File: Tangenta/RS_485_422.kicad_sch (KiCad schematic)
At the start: 37 parts, among them Q3 BSS138, U21 TPCDSOT23-SM712, U22 TPCDSOT23-SM712

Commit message: ...
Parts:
- added C1 (x2): 10nF, Capacitor_SMD:C_0402_1005Metric, symbol Device:C_Small
- added J15: Conn_01x06_Pin, Connector_PinHeader_2.54mm:PinHeader_1x06_P2.54mm_Vertical, symbol Connector:Conn_01x06_Pin
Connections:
- net 5V: now also C1.2, C1.2
- net CTS_2_H: now also J15.3 (Pin_3)
- net GNDREF: now also C1.1, C1.1, J15.5 (Pin_5), J15.6 (Pin_6)
- net RTS_2_H: now also J15.2 (Pin_2)
- net RXD_2_H: now also J15.1 (Pin_1)
- net TXD_2_H: now also J15.4 (Pin_4)
- net RS485_CH_1.N: no longer names the net of R2.1, R2.1
- net RS485_CH_1.N: no longer U21.1
- net RS485_CH_1.P: no longer names the net of R2.1, R2.2
- net RS485_CH_1.P: no longer U21.2
- net RS485_CH_2.N: no longer names the net of R2.1, R2.1
- net RS485_CH_2.N: no longer U22.1
- net RS485_CH_2.P: no longer names the net of R2.1, R2.2
- net RS485_CH_2.P: no longer U22.2
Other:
- note added: "For future use"
- moved on the sheet: C1, R2, U21, U22

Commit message: ...
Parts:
- added U19: ADM2582E, Package_SO:SOIC-20W_7.5x12.8mm_P1.27mm, symbol Interface_UART:ADM2582E
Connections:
- net 5V: now also U19.2 (VCC), U19.8 (VCC); no longer C1.2, C1.2, C1.2
- net A: now also R2.2, U19.18 (A); no longer R2.2, R2.2
- net B: now also R2.2, U19.17 (B); no longer R2.2, R2.2
- net CTS_1_H: now also U19.6 (DE)
- net GNDREF: now also U19.1 (GND1), U19.10 (GND1), U19.3 (GND1), U19.9 (GND1); no longer C1.1, C1.1, C1.1, U21.3, U22.3
- net RTS_1_H: now also U19.5 (~{RE})
- net RXD_1_H: now also U19.4 (RxD)
- net TXD_1_H: now also U19.7 (TxD)
- net RS.R_P: now reaches R2.1, R2.1
- net RS.R_P: now also U22.1
- net RS.R_N: now reaches R2.1, R2.2
- net RS.R_N: now also U22.2
- net RS.D_P: now reaches R2.1, R2.2
- net RS.D_P: now also U21.2
- net RS.D_N: now reaches R2.1, R2.1
- net RS.D_N: now also U21.1
- new net RS_ISO_5V: C1.2, C1.2, C1.2, U19.12 (Visoout), U19.19 (Visoin)
- new net RS_ISO_GND: C1.1, C1.1, C1.1, U19.11 (GND2), U19.14 (GND2), U19.16 (GND2), U19.20 (GND2), U21.3, U22.3
- new net Y: R2.2, U19.13 (Y)
- new net Z: R2.2, U19.15 (Z)
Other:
- moved on the sheet: C1, J15, R2, U21, U22

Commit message: RS-485/422 revisited.
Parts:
- added J22: Conn_01x02_Pin, Connector_PinHeader_2.54mm:PinHeader_1x02_P2.54mm_Vertical, symbol Connector:Conn_01x02_Pin
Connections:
- net RS_ISO_GND: now also J22.2 (Pin_2)
- new net RS_CONN_GND: J22.1 (Pin_1)
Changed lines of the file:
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@@
+    (stroke (width 0) (type default))
+  )
+  (wire (pts (xy 248.92 135.89) (xy 252.73 135.89))
     (stroke (width 0) (type default))
   )
@@
     (stroke (width 0) (type default))
   )
+  (wire (pts (xy 246.38 135.89) (xy 227.965 135.89))
+    (stroke (width 0) (type default))
+  )
   (wire (pts (xy 133.985 42.545) (xy 137.795 42.545))
     (stroke (width 0) (type default))
@@
     (effects (font (size 1.27 1.27)) (justify right bottom))
   )
+  (label "RS_ISO_GND" (at 227.965 135.89 0) (fields_autoplaced)
+    (effects (font (size 1.27 1.27)) (justify left bottom))
+  )
   (label "5V" (at 42.545 27.305 0) (fields_autoplaced)
     (effects (font (size 1.27 1.27)) (justify left bottom))
@@
   (label "RS_ISO_GND" (at 243.84 41.91 180) (fields_autoplaced)
     (effects (font (size 1.27 1.27)) (justify right bottom))
+  )
+  (hierarchical_label "RS_CONN_GND" (shape bidirectional) (at 252.73 135.89 0) (fields_autoplaced)
+    (effects (font (size 1.27 1.27)) (justify left))
   )
   (hierarchical_label "UART_1{RXD TXD RTS CTS}" (shape input) (at 43.18 60.325 180) (fields_autoplaced)
@@
         )
       )
+    )
+  )
+  (symbol (lib_id "Connector:Conn_01x02_Pin") (at 248.92 130.81 270) (unit 1)
+    (in_bom yes) (on_board yes) (dnp no)
+    (property "Reference" "J22" (at 245.745 129.54 90)
+      (effects (font (size 1.27 1.27)) (justify left))
+    )
+    (property "Value" "Conn_01x02_Pin" (at 250.19 132.715 90)
+      (effects (font (size 1.27 1.27)) (justify left) hide)
+    )
+    (property "Footprint" "Connector_PinHeader_2.54mm:PinHeader_1x02_P2.54mm_Vertical" (at 248.92 130.81 0)
+      (effects (font (size 1.27 1.27)) hide)
+    )
+    (property "Datasheet" "~" (at 248.92 130.81 0)
+      (effects (font (size 1.27 1.27)) hide)
+    )
+    (pin "1")
+    (pin "2")
+    (instances
+      (project "Tangenta"
+        (path "/358d1bcf-7599-4352-8c4d-baa18a5f09e6/98e3b24f-9927-4339-b8fd-9deea91a522a"
+          (reference "J22") (unit 1)
+        )
+      )

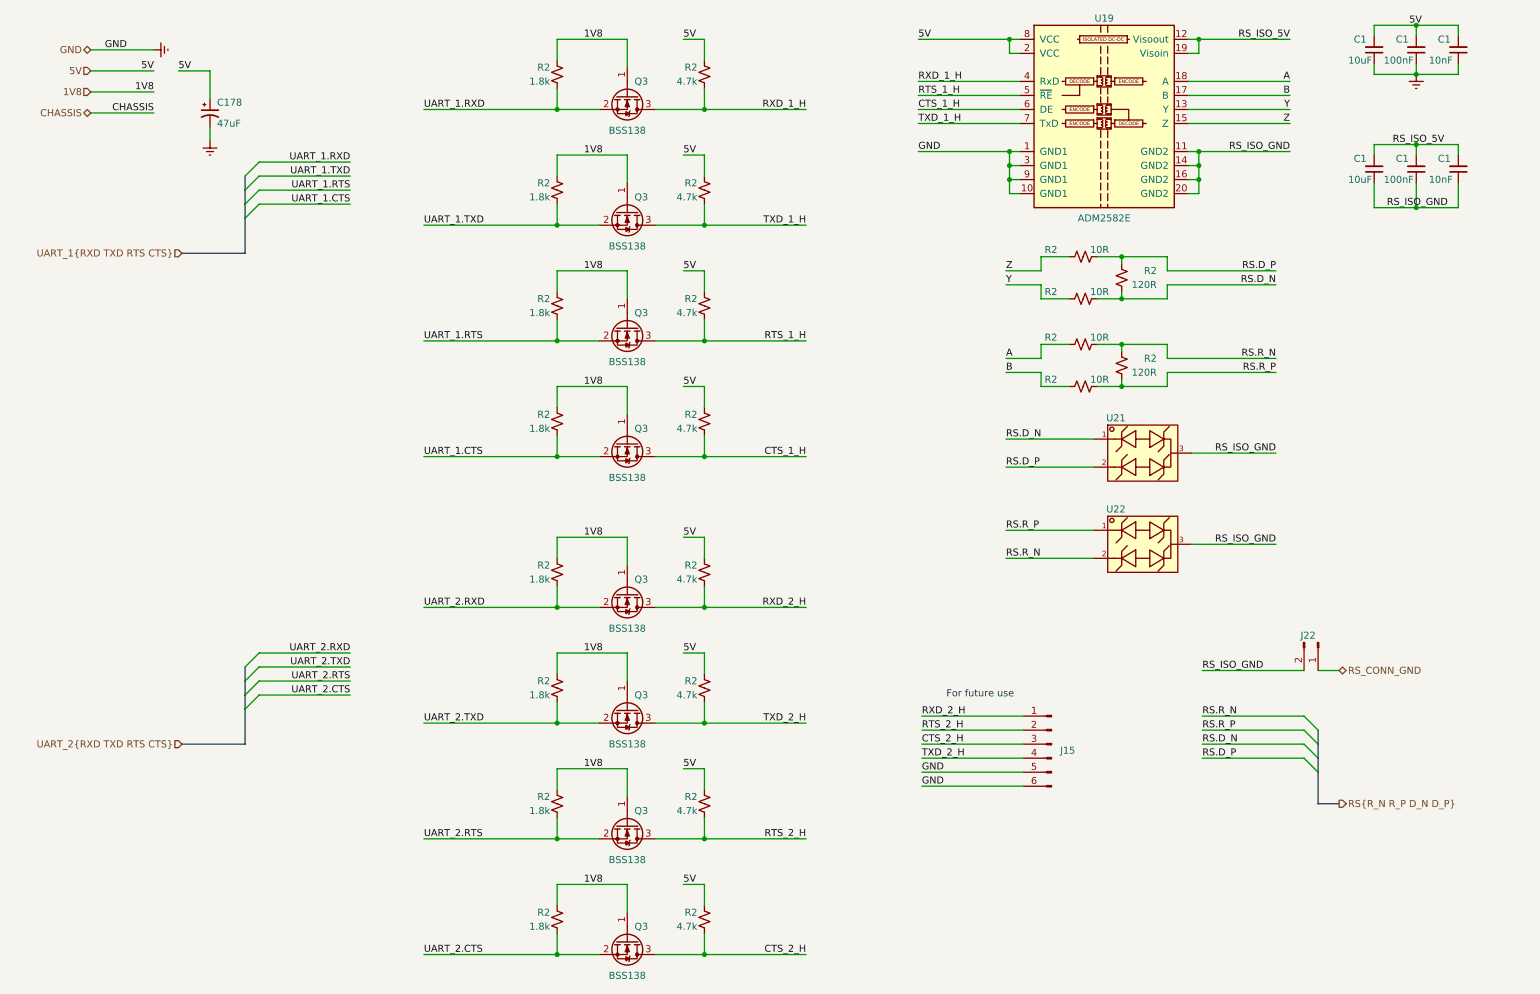
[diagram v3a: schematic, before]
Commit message: RS-485/422 schematics fine-tuned.
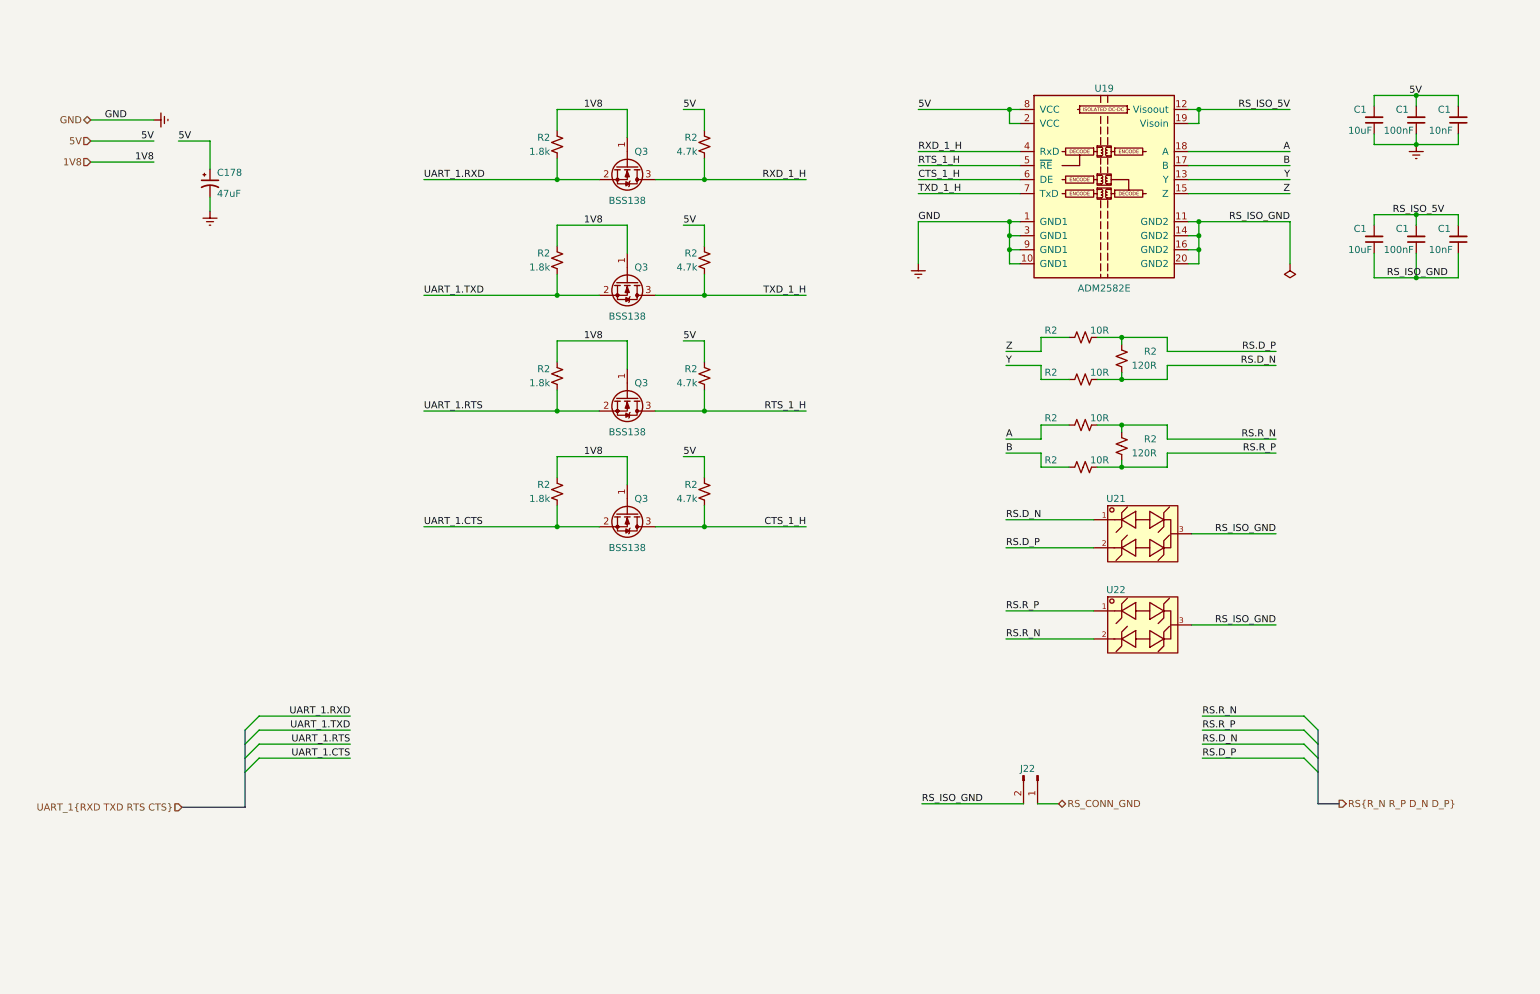
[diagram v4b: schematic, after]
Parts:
- removed J15: Conn_01x06_Pin, Connector_PinHeader_2.54mm:PinHeader_1x06_P2.54mm_Vertical, symbol Connector:Conn_01x06_Pin
- removed Q3 (x4): BSS138, Package_TO_SOT_SMD:SOT-23, symbol Transistor_FET:BSS138
- removed R2 (x4): 4.7k, Resistor_SMD:R_0402_1005Metric, symbol Device:R_Small_US
- removed R2 (x4): 1.8k, Resistor_SMD:R_0402_1005Metric, symbol Device:R_Small_US
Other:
- note removed: "For future use"
- moved on the sheet: C1, C178, J22, Q3, R2, U19, U21, U22

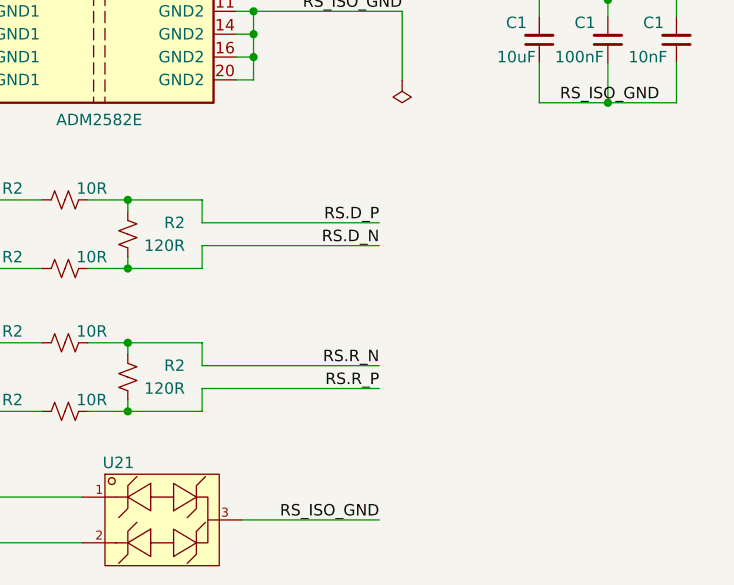
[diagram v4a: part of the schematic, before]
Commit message: Adding 0Rs for RS-485 configuration.
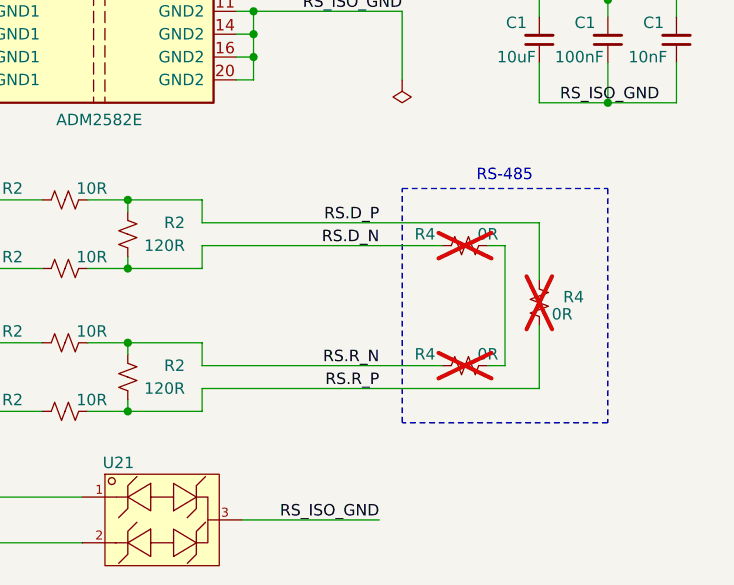
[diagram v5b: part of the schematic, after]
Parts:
- added R4 (x3): 0R, Resistor_SMD:R_0603_1608Metric, symbol Device:R_Small_US
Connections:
- net RS.D_N: now also R4.2
- net RS.D_P: now also R4.1
- net RS.R_N: now also R4.2
- net RS.R_P: now also R4.2
- new net: R4.1, R4.1
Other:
- note added: "RS-485"
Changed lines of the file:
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@@
     (stroke (width 0) (type default))
   )
-  (wire (pts (xy 221.615 93.98) (xy 241.3 93.98))
+  (wire (pts (xy 221.615 93.98) (xy 248.285 93.98))
     (stroke (width 0) (type default))
   )
@@
     (stroke (width 0) (type default))
   )
-  (wire (pts (xy 221.615 78.105) (xy 241.3 78.105))
+  (wire (pts (xy 221.615 78.105) (xy 259.08 78.105))
+    (stroke (width 0) (type default))
+  )
+  (wire (pts (xy 255.27 80.645) (xy 255.27 93.98))
     (stroke (width 0) (type default))
   )
@@
     (stroke (width 0) (type default))
   )
-  (wire (pts (xy 221.615 96.52) (xy 241.3 96.52))
+  (wire (pts (xy 221.615 96.52) (xy 259.08 96.52))
     (stroke (width 0) (type default))
   )
@@
     (stroke (width 0) (type default))
   )
-  (wire (pts (xy 221.615 80.645) (xy 241.3 80.645))
+  (wire (pts (xy 221.615 80.645) (xy 248.285 80.645))
     (stroke (width 0) (type default))
   )
@@
     (stroke (width 0) (type default))
   )
+  (wire (pts (xy 253.365 80.645) (xy 255.27 80.645))
+    (stroke (width 0) (type default))
+  )
   (bus (pts (xy 43.18 160.655) (xy 54.61 160.655))
     (stroke (width 0) (type default))
@@
     (stroke (width 0) (type default))
   )
+  (wire (pts (xy 259.08 89.535) (xy 259.08 96.52))
+    (stroke (width 0) (type default))
+  )
   (wire (pts (xy 221.615 75.565) (xy 221.615 78.105))
     (stroke (width 0) (type default))
@@
     (stroke (width 0) (type default))
   )
+  (wire (pts (xy 255.27 93.98) (xy 253.365 93.98))
+    (stroke (width 0) (type default))
+  )
   (wire (pts (xy 198.755 80.645) (xy 198.755 83.185))
     (stroke (width 0) (type default))
@@
   (wire (pts (xy 192.405 93.98) (xy 198.755 93.98))
     (stroke (width 0) (type default))
+  )
+  (wire (pts (xy 259.08 84.455) (xy 259.08 78.105))
+    (stroke (width 0) (type default))
+  )
+  (rectangle (start 243.84 74.295) (end 266.7 100.33)
+    (stroke (width 0) (type dash))
+    (fill (type none))
+  )
+  (text "RS-485" (at 252.095 73.66 0)
+    (effects (font (size 1.27 1.27)) (justify left bottom))
   )
   (label "GND" (at 176.53 54.61 0) (fields_autoplaced)
@@
     )
   )
+  (symbol (lib_id "Device:R_Small_US") (at 250.825 80.645 270) (unit 1)
+    (in_bom no) (on_board yes) (dnp yes)
+    (property "Reference" "R4" (at 246.38 79.375 90)
+      (effects (font (size 1.27 1.27)))
+    )
+    (property "Value" "0R" (at 253.365 79.375 90)
+      (effects (font (size 1.27 1.27)))
+    )
+    (property "Footprint" "Resistor_SMD:R_0603_1608Metric" (at 250.825 80.645 0)
+      (effects (font (size 1.27 1.27)) hide)
+    )
+    (property "Datasheet" "~" (at 250.825 80.645 0)
+      (effects (font (size 1.27 1.27)) hide)
+    )
+    (pin "1")
+    (pin "2")
+    (instances
+      (project "Tangenta"
+        (path "/358d1bcf-7599-4352-8c4d-baa18a5f09e6/8215796b-9611-4f43-bcc5-319f8414b8a6"
+          (reference "R4") (unit 1)
+        )
+        (path "/358d1bcf-7599-4352-8c4d-baa18a5f09e6/98e3b24f-9927-4339-b8fd-9deea91a522a"
+          (reference "R171") (unit 1)
+        )
+      )
+    )
+  )
   (symbol (lib_id "Device:R_Small_US") (at 137.795 82.55 180) (unit 1)
     (in_bom yes) (on_board yes) (dnp no)
@@
         (path "/358d1bcf-7599-4352-8c4d-baa18a5f09e6/98e3b24f-9927-4339-b8fd-9deea91a522a"
           (reference "R170") (unit 1)
+        )
+      )
+    )
+  )
+  (symbol (lib_id "Device:R_Small_US") (at 259.08 86.995 0) (unit 1)
+    (in_bom no) (on_board yes) (dnp yes)
+    (property "Reference" "R4" (at 262.89 86.36 0)
+      (effects (font (size 1.27 1.27)))
+    )
+    (property "Value" "0R" (at 261.62 88.265 0)
+      (effects (font (size 1.27 1.27)))
+    )
+    (property "Footprint" "Resistor_SMD:R_0603_1608Metric" (at 259.08 86.995 0)
+      (effects (font (size 1.27 1.27)) hide)
+    )
+    (property "Datasheet" "~" (at 259.08 86.995 0)
+      (effects (font (size 1.27 1.27)) hide)
+    )
+    (pin "1")
+    (pin "2")
+    (instances
+      (project "Tangenta"
+        (path "/358d1bcf-7599-4352-8c4d-baa18a5f09e6/8215796b-9611-4f43-bcc5-319f8414b8a6"
+          (reference "R4") (unit 1)
+        )
+        (path "/358d1bcf-7599-4352-8c4d-baa18a5f09e6/98e3b24f-9927-4339-b8fd-9deea91a522a"
+          (reference "R173") (unit 1)
         )
       )
@@
         )
       )
+    )
+  )
+  (symbol (lib_id "Device:R_Small_US") (at 250.825 93.98 270) (unit 1)
+    (in_bom no) (on_board yes) (dnp yes)
+    (property "Reference" "R4" (at 246.38 92.71 90)
+      (effects (font (size 1.27 1.27)))
+    )
+    (property "Value" "0R" (at 253.365 92.71 90)
+      (effects (font (size 1.27 1.27)))
+    )
+    (property "Footprint" "Resistor_SMD:R_0603_1608Metric" (at 250.825 93.98 0)
+      (effects (font (size 1.27 1.27)) hide)
+    )
+    (property "Datasheet" "~" (at 250.825 93.98 0)
+      (effects (font (size 1.27 1.27)) hide)
+    )
+    (pin "1")
+    (pin "2")
+    (instances
+      (project "Tangenta"
+        (path "/358d1bcf-7599-4352-8c4d-baa18a5f09e6/8215796b-9611-4f43-bcc5-319f8414b8a6"
+          (reference "R4") (unit 1)
+        )
+        (path "/358d1bcf-7599-4352-8c4d-baa18a5f09e6/98e3b24f-9927-4339-b8fd-9deea91a522a"
+          (reference "R172") (unit 1)
+        )
+      )
